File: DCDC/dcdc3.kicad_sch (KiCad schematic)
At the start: 8 parts

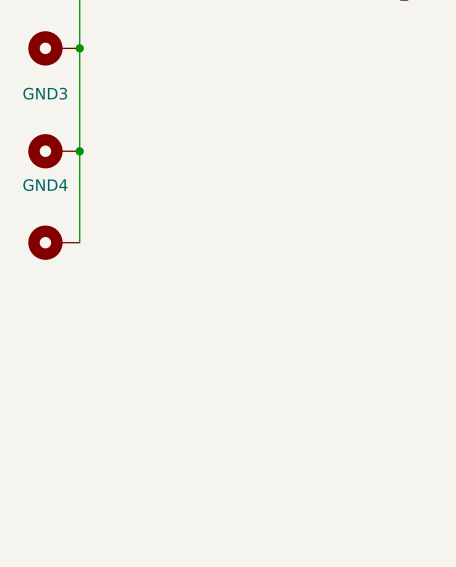
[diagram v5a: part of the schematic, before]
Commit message: 3 modules of DCDC, hinge
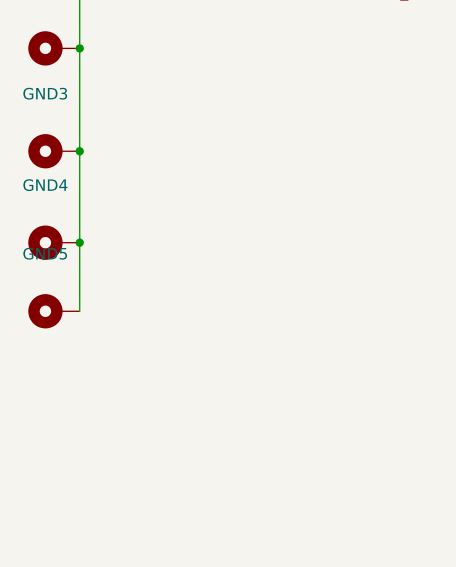
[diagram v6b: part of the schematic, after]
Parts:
- added GND5: ~, MountingHole:MountingHole_2.7mm_M2.5_Pad_Via, symbol Mechanical:MountingHole_Pad
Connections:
- net 12V/GND: now also GND5.1
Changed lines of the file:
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@@
+	)
+	(junction
+		(at 29.21 130.81)
+		(diameter 0)
+		(color 0 0 0 0)
 	)
 	(junction
@@
 		(pts
 			(xy 52.07 69.85) (xy 34.29 69.85)
+		)
+		(stroke
+			(width 0)
+			(type default)
+		)
+	)
+	(wire
+		(pts
+			(xy 29.21 130.81) (xy 29.21 138.43)
 		)
 		(stroke
@@
 					(unit 1)
 				)
+			)
+		)
+	)
+	(symbol
+		(lib_id "Mechanical:MountingHole_Pad")
+		(at 26.67 138.43 90)
+		(unit 1)
+		(exclude_from_sim yes)
+		(in_bom yes)
+		(on_board yes)
+		(dnp no)
+		(fields_autoplaced yes)
+		(property "Reference" "GND5"
+			(at 25.4 132.08 90)
+			(effects
+				(font
+					(size 1.27 1.27)
+				)
+			)
+		)
+		(property "Value" "~"
+			(at 25.4 134.62 90)
+			(effects
+				(font
+					(size 1.27 1.27)
+				)
+				(hide yes)
+			)
+		)
+		(property "Footprint" "MountingHole:MountingHole_2.7mm_M2.5_Pad_Via"
+			(at 26.67 138.43 0)
+			(effects
+				(font
+					(size 1.27 1.27)
+				)
+				(hide yes)
+			)
+		)
+		(property "Datasheet" "~"
+			(at 26.67 138.43 0)
+			(effects
+				(font
+					(size 1.27 1.27)
+				)
+				(hide yes)
+			)
+		)
+		(property "Description" "Mounting Hole with connection"
+			(at 26.67 138.43 0)
+			(effects
+				(font
+					(size 1.27 1.27)
+				)
+				(hide yes)
+			)
+		)
+		(pin "1"
+		)
+		(instances
+			(project "dcdc3"
+				(path "/074a9d0b-fc12-4aa8-94e4-356d74449fb4"
+					(reference "GND5")
+					(unit 1)
+				)
